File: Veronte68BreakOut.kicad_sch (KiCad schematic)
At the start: 11 parts, among them J1 DC37_Receptacle_MountingHoles, J10 Barrel_Jack_Switch, J11 Barrel_Jack_Switch, J2 DC37_Receptacle_MountingHoles, J3 DE9_Receptacle_MountingHoles, J4 Conn_01x19, J5 Conn_01x11, J6 Conn_01x19, J7 Conn_01x11, J8 Conn_01x05, J9 Conn_01x03

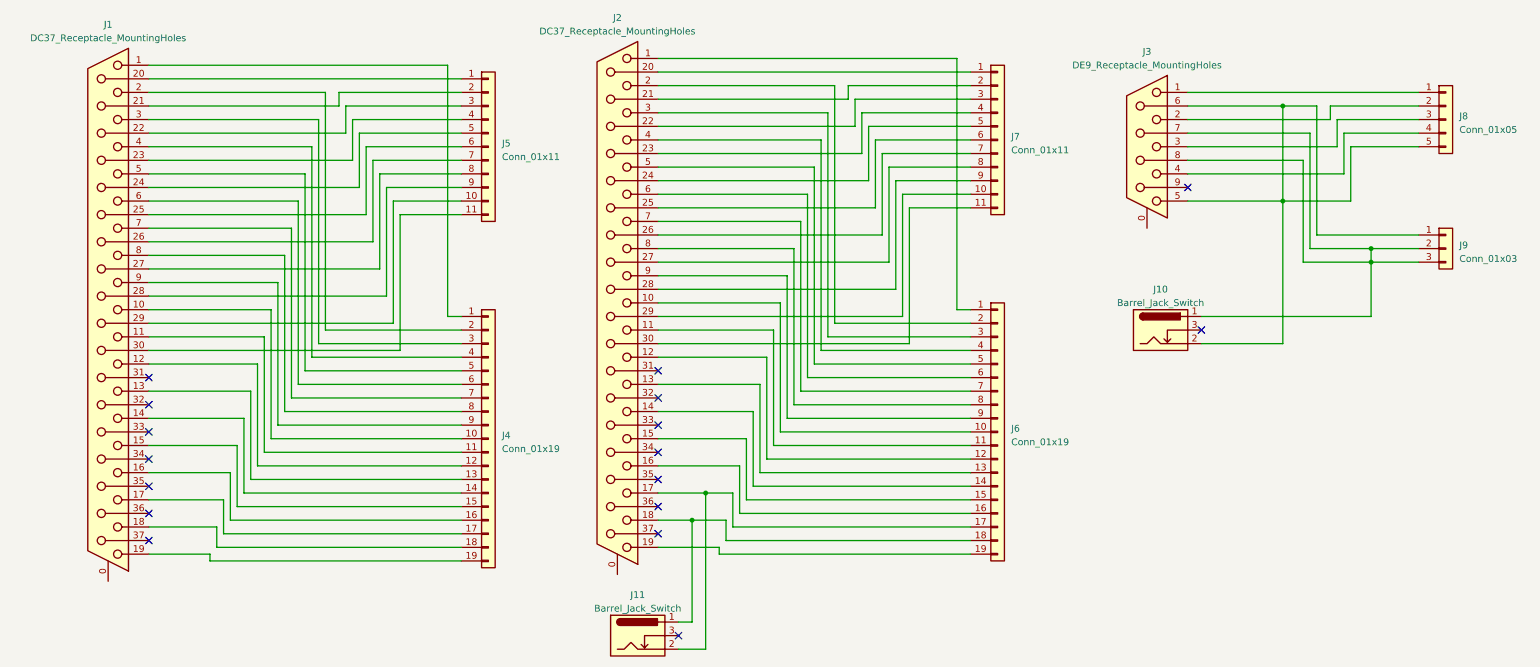
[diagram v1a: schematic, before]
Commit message: add v1.3
- change 60/61/62 pin
- change number of pin header
- add GND and solid GND pattern
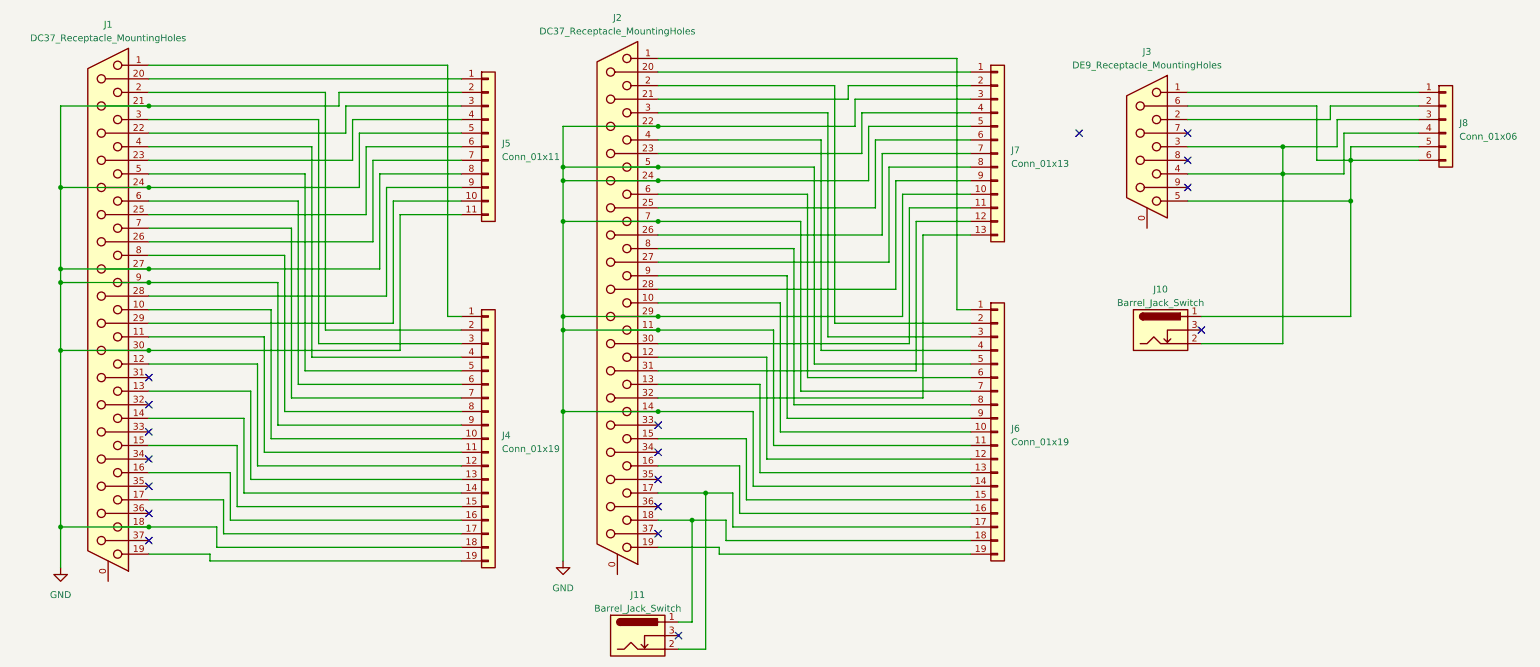
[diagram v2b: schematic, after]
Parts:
- removed J7: Conn_01x11, Connector_PinHeader_2.54mm:PinHeader_1x11_P2.54mm_Vertical, symbol Connector_Generic:Conn_01x11
- removed J8: Conn_01x05, Connector_PinHeader_2.54mm:PinHeader_1x05_P2.54mm_Vertical, symbol Connector_Generic:Conn_01x05
- removed J9: Conn_01x03, Connector_PinHeader_2.54mm:PinHeader_1x03_P2.54mm_Vertical, symbol Connector_Generic:Conn_01x03
- added J7: Conn_01x13, Connector_PinHeader_2.54mm:PinHeader_1x13_P2.54mm_Vertical, symbol Connector_Generic:Conn_01x13
- added J8: Conn_01x06, Connector_PinHeader_2.54mm:PinHeader_1x06_P2.54mm_Vertical, symbol Connector_Generic:Conn_01x06
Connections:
- net at J3.5, J3.6: now also J10.1, J8.5 (Pin_5), J8.6 (Pin_6); no longer J10.2
- net at J2.20: now also J7.1 (Pin_1)
- net GND: now reaches J2.29
- net GND: now also J1.18, J1.21, J1.24, J1.27, J1.30, J1.9, J2.11, J2.14, J2.22, J2.24, J2.5, J2.7, J4.18 (Pin_18), J4.9 (Pin_9), J5.11 (Pin_11), J5.2 (Pin_2), J5.5 (Pin_5), J5.8 (Pin_8), J6.11 (Pin_11), J6.14 (Pin_14), J6.5 (Pin_5), J6.7 (Pin_7), J7.10 (Pin_10), J7.3 (Pin_3), J7.5 (Pin_5)
- net at J2.30: now also J7.11 (Pin_11)
- net at J2.21: now also J7.2 (Pin_2)
- net at J2.23: now also J7.4 (Pin_4)
- net at J2.25: now also J7.6 (Pin_6)
- net at J2.26: now also J7.7 (Pin_7)
- net at J2.27: now also J7.8 (Pin_8)
- net at J2.28: now also J7.9 (Pin_9)
- net at J3.1: now also J8.1 (Pin_1)
- net at J3.2: now also J8.2 (Pin_2)
- net at J3.3: now also J10.2, J3.4, J8.3 (Pin_3), J8.4 (Pin_4)
- net at J2.31: now also J7.12 (Pin_12)
- net at J2.32: now also J7.13 (Pin_13)
- now unconnected: J3.7, J3.8
- no-connect marks 17 -> 18

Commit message: add v2.0
add v2.0
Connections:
- net GND: no longer J2.22, J7.3 (Pin_3)
- new net: J2.22, J7.3 (Pin_3)
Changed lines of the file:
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@@
   (title_block
     (title "Veronte68 -> 2.54mm Breakout")
-    (date "2023-07-07")
-    (rev "v1.3.0")
+    (date "2023-08-01")
+    (rev "v2.0")
     (company "teTra aviation corp.")
     (comment 1 "change 60/61/62 pin")
     (comment 2 "change number of pin header")
     (comment 3 "add GND")
+    (comment 4 "fix 52 pin")
   )
   (junction (at 33.02 90.17) (diameter 0) (color 0 0 0 0)
@@
   (junction (at 16.51 90.17) (diameter 0) (color 0 0 0 0)
   )
-  (junction (at 110.49 55.88) (diameter 0) (color 0 0 0 0)
-  )
   (junction (at 16.51 74.93) (diameter 0) (color 0 0 0 0)
   )
   (junction (at 16.51 59.69) (diameter 0) (color 0 0 0 0)
-  )
-  (junction (at 128.27 48.26) (diameter 0) (color 0 0 0 0)
   )
   (junction (at 257.81 62.23) (diameter 0) (color 0 0 0 0)
@@
     (stroke (width 0) (type default))
   )
-  (wire (pts (xy 110.49 48.26) (xy 110.49 55.88))
-    (stroke (width 0) (type default))
-  )
   (wire (pts (xy 44.45 129.54) (xy 91.44 129.54))
     (stroke (width 0) (type default))
@@
     (stroke (width 0) (type default))
   )
-  (wire (pts (xy 128.27 48.26) (xy 110.49 48.26))
-    (stroke (width 0) (type default))
-  )
